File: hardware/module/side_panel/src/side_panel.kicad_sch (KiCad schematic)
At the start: 34 parts, among them J1 Top Connector, J2 Bottom Connecor, J3 Conn_01x05, J4 Conn_01x09, M1 GA12-N20 12V 100rpm, Q1 AP2302B, U1 QRE1113GR, U10 NUP4202, U2 QRE1113GR, U3 QRE1113GR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

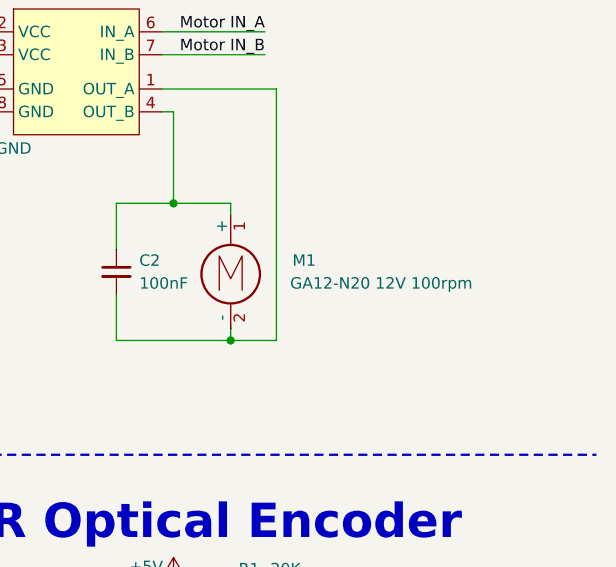
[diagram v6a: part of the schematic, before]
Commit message: update side panel schematic motor RPM
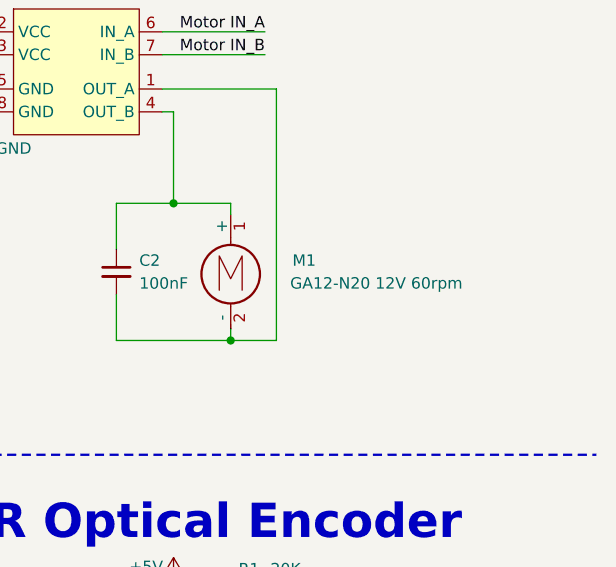
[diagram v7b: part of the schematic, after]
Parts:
- M1: value GA12-N20 12V 100rpm -> GA12-N20 12V 60rpm
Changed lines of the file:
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@@
 		(title "Side Panel")
 		(date "${DATE}")
-		(rev "4.1.2")
+		(rev "4.1.3")
 		(company "OpenFlap")
 		(comment 1 "${GIT_TAG}")
@@
 			)
 		)
-		(property "Value" "GA12-N20 12V 100rpm"
+		(property "Value" "GA12-N20 12V 60rpm"
 			(at 162.814 69.85 0)
 			(effects

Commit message: wip
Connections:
- net IR Sens Ch 1: now also U7.19 (PA0); no longer U7.1 (PA2)
- net IR Sens Ch 2: now also U7.4 (PA5); no longer U7.2 (PA3)
- net IR Sens Ch 5: now also U7.1 (PA2); no longer U7.19 (PA0)
- net IR Sens Ch 6: now also U7.2 (PA3); no longer U7.4 (PA5)
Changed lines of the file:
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@@
 		)
 	)
-	(label "IR Sens Ch 2"
+	(label "IR Sens Ch 6"
 		(at 34.29 44.45 0)
 		(fields_autoplaced yes)
@@
 		)
 	)
-	(label "IR Sens Ch 5"
+	(label "IR Sens Ch 1"
 		(at 34.29 36.83 0)
 		(fields_autoplaced yes)
@@
 		)
 	)
-	(label "IR Sens Ch 6"
+	(label "IR Sens Ch 2"
 		(at 34.29 49.53 0)
 		(fields_autoplaced yes)
@@
 		)
 	)
-	(label "IR Sens Ch 1"
+	(label "IR Sens Ch 5"
 		(at 34.29 41.91 0)
 		(fields_autoplaced yes)
